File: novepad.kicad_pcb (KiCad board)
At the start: 2 copper layers, 99 x 59.5 mm, 16 parts, among them J101 NOVENA_LCD_CONN, J102 LP097QX1_CONN, J401 MOLEX_502250-8037, J402 MOLEX_502250-8037, U301 IT6251, U401 FT5816LPC

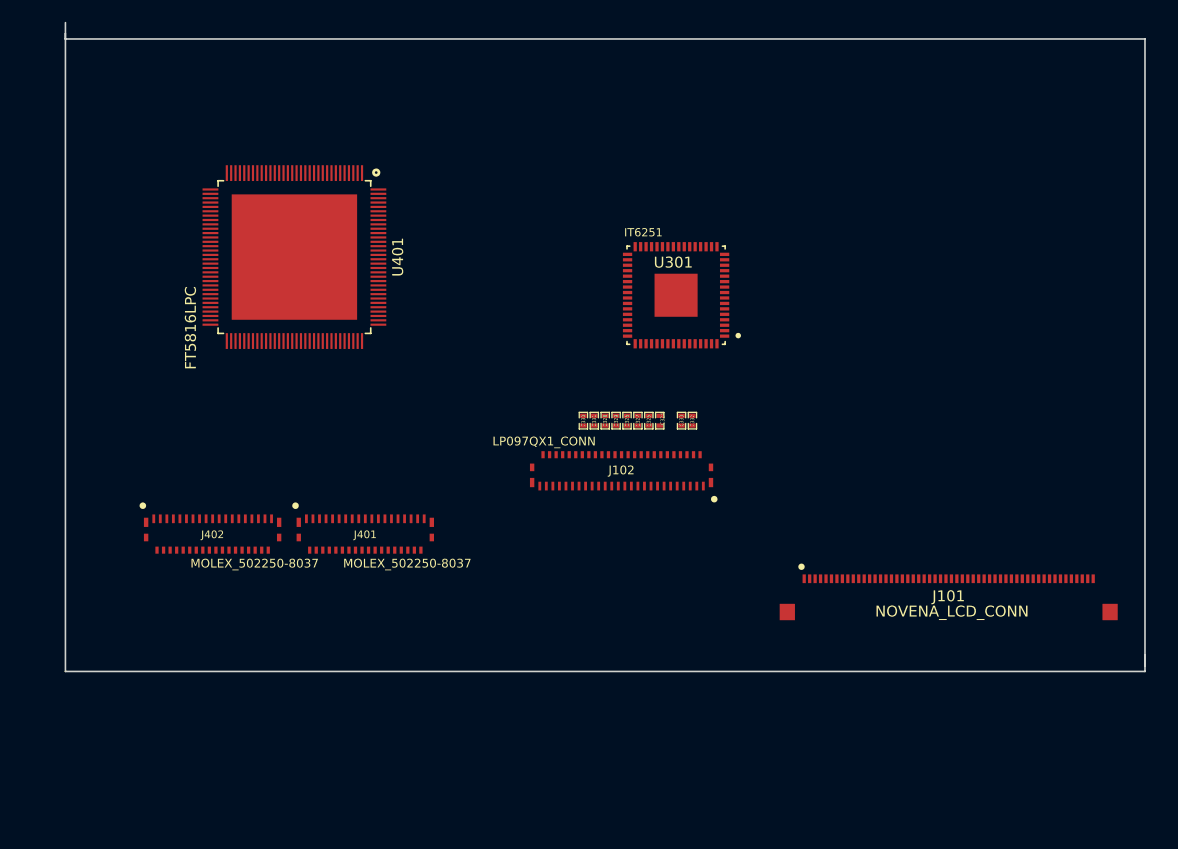
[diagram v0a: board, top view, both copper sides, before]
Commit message: First attempt at routing the high speed differential traces
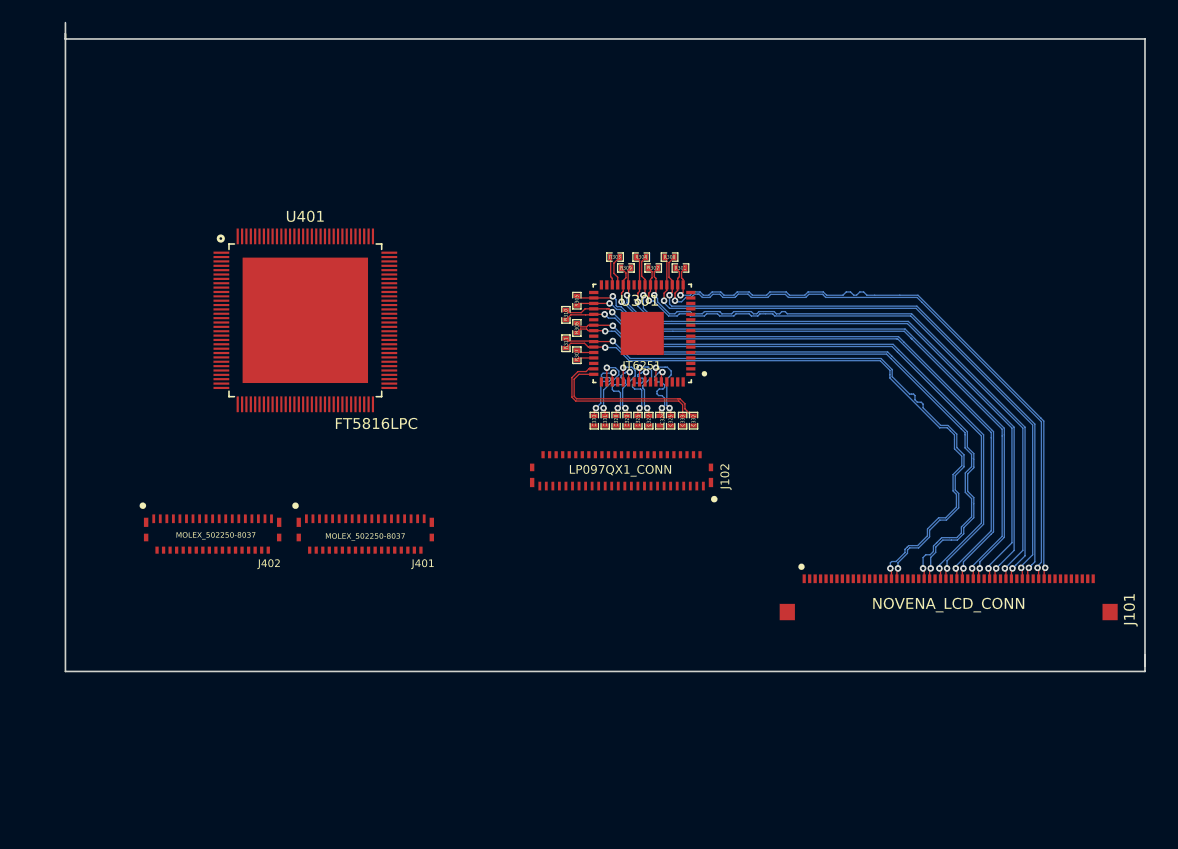
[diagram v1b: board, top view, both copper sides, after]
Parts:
- added R301: 100R 1%, SMD_Packages:SMD-0402_r, F.Cu at (144.4, 118.0)
- added R302: 100R 1%, SMD_Packages:SMD-0402_r, F.Cu at (141.9, 118.0)
- added R303: 100R 1%, SMD_Packages:SMD-0402_r, F.Cu at (138.4, 117.0)
- added R304: 100R 1%, SMD_Packages:SMD-0402_r, F.Cu at (140.8, 117.0)
- added R305: 100R 1%, SMD_Packages:SMD-0402_r, F.Cu at (134.9, 121.0)
- added R306: 100R 1%, SMD_Packages:SMD-0402_r, F.Cu at (134.9, 123.5)
- added R307: 100R 1%, SMD_Packages:SMD-0402_r, F.Cu at (134.9, 126.0)
- added R308: 100R 1%, SMD_Packages:SMD-0402_r, F.Cu at (143.4, 117.0)
- added R309: 100R 1%, SMD_Packages:SMD-0402_r, F.Cu at (139.4, 118.0)
- added R310: 100R 1%, SMD_Packages:SMD-0402_r, F.Cu at (133.9, 122.3)
- added R311: 100R 1%, SMD_Packages:SMD-0402_r, F.Cu at (133.9, 124.9)
- moved U401 5.89 mm to (110.0, 122.8), turned to 0 degrees
- moved U301 4.68 mm to (140.9, 124.0)
- moved C325 2.00 mm to (143.5, 132.0)
- moved C326 1.00 mm to (140.5, 132.0)
- moved C327 1.00 mm to (141.5, 132.0)
- moved C328 1.00 mm to (138.5, 132.0)
- moved C329 1.00 mm to (139.5, 132.0)
- moved C330 1.00 mm to (136.5, 132.0)
- moved C331 1.00 mm to (137.5, 132.0)
- moved C332 0.10 mm to (145.6, 132.0)
- moved C333 0.10 mm to (144.6, 132.0)
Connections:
- J101 pad 20: Net-(J101-Pad20) -> (no net)
- J101 pad 21: Net-(J101-Pad21) -> (no net)
- J101 pad 51: Net-(J101-Pad51) -> (no net)
- J101 pad 52: Net-(J101-Pad52) -> (no net)
- J101 pad 53: Net-(J101-Pad53) -> (no net)
- J101 pad 54: Net-(J101-Pad54) -> (no net)
- J102 pad 13: Net-(J102-Pad13) -> (no net)
- J102 pad 17: Net-(J102-Pad17) -> (no net)
- J102 pad 21: Net-(J102-Pad21) -> (no net)
- J102 pad 25: Net-(J102-Pad25) -> (no net)
- J102 pad 44: Net-(J102-Pad44) -> (no net)
- J102 pad 47: Net-(J102-Pad47) -> (no net)
- J102 pad 50: Net-(J102-Pad50) -> (no net)
- U301 pad 1: Net-(U301-Pad1) -> (no net)
- U301 pad 10: Net-(U301-Pad10) -> (no net)
- U301 pad 8: Net-(U301-Pad8) -> (no net)
- U301 pad 9: Net-(U301-Pad9) -> (no net)
- U401 pad 126: Net-(U401-Pad126) -> (no net)
- U401 pad 127: Net-(U401-Pad127) -> (no net)
- U401 pad 128: Net-(U401-Pad128) -> (no net)
- U401 pad 37: Net-(U401-Pad37) -> (no net)
- U401 pad 38: Net-(U401-Pad38) -> (no net)
- U401 pad 40: Net-(U401-Pad40) -> (no net)
- U401 pad 41: Net-(U401-Pad41) -> (no net)
- U401 pad 42: Net-(U401-Pad42) -> (no net)
- U401 pad 43: Net-(U401-Pad43) -> (no net)
- U401 pad 44: Net-(U401-Pad44) -> (no net)
- U401 pad 45: Net-(U401-Pad45) -> (no net)
- U401 pad 47: Net-(U401-Pad47) -> (no net)
- U401 pad 68: Net-(U401-Pad68) -> (no net)
- U401 pad 77: Net-(U401-Pad77) -> (no net)
- U401 pad 78: Net-(U401-Pad78) -> (no net)
- U401 pad 79: Net-(U401-Pad79) -> (no net)
- U401 pad 80: Net-(U401-Pad80) -> (no net)
- U401 pad 83: Net-(U401-Pad83) -> (no net)
- U401 pad 86: Net-(U401-Pad86) -> (no net)
- U401 pad 87: Net-(U401-Pad87) -> (no net)
- U401 pad 88: Net-(U401-Pad88) -> (no net)
- U401 pad 89: Net-(U401-Pad89) -> (no net)
- U401 pad 93: Net-(U401-Pad93) -> (no net)
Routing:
- net /LVDS to eDP Conversion/LVDS1_0_N: track 0.00 -> 58.5 mm, vias 0 -> 2
- net /LVDS to eDP Conversion/LVDS0_3_P: track 0.00 -> 58.4 mm, vias 0 -> 2
- net /LVDS to eDP Conversion/LVDS_CLK_P: track 0.00 -> 58.4 mm, vias 0 -> 2
- net /LVDS to eDP Conversion/LVDS_CLK_N: track 0.00 -> 58.2 mm, vias 0 -> 2
- net /LVDS to eDP Conversion/LVDS1_1_N: track 0.00 -> 58.0 mm, vias 0 -> 2
- net /LVDS to eDP Conversion/LVDS1_0_P: track 0.00 -> 57.8 mm, vias 0 -> 2
- net /LVDS to eDP Conversion/LVDS1_1_P: track 0.00 -> 57.7 mm, vias 0 -> 2
- net /LVDS to eDP Conversion/LVDS0_0_P: track 0.00 -> 57.6 mm, vias 0 -> 2
- net /LVDS to eDP Conversion/LVDS1_3_N: track 0.00 -> 57.6 mm, vias 0 -> 2
- net /LVDS to eDP Conversion/LVDS0_2_P: track 0.00 -> 57.5 mm, vias 0 -> 2
- net /LVDS to eDP Conversion/LVDS0_3_N: track 0.00 -> 57.5 mm, vias 0 -> 2
- net /LVDS to eDP Conversion/LVDS0_1_P: track 0.00 -> 57.5 mm, vias 0 -> 2
- net /LVDS to eDP Conversion/LVDS1_3_P: track 0.00 -> 57.3 mm, vias 0 -> 2
- net /LVDS to eDP Conversion/LVDS0_1_N: track 0.00 -> 57.3 mm, vias 0 -> 2
- net /LVDS to eDP Conversion/LVDS0_0_N: track 0.00 -> 57.2 mm, vias 0 -> 2
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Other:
- copper layers 2 -> 4
- net class Backlight added: clearance 0.2, trace_width 0.3, via_dia 0.7, via_drill 0.4
- net class Default: clearance 0.254 -> 0.2; trace_width 0.254 -> 0.2; via_dia 0.889 -> 0.7; via_drill 0.635 -> 0.4
- net class LVDS_LM3 added: clearance 0.1, trace_width 0.1, via_dia 0.6, via_drill 0.3
- net class LVDS_Unused added: clearance 0.1, trace_width 0.1, via_dia 0.7, via_drill 0.4
- net class Power added: clearance 0.3, trace_width 0.5, via_dia 1.2, via_drill 0.5
- net class eDP_ACC_LM0.2 added: clearance 0.1, trace_width 0.1, via_dia 0.6, via_drill 0.3
- net class eDP_AUX_LM0.5 added: clearance 0.1, trace_width 0.1, via_dia 0.6, via_drill 0.3
- net class eDP_LM0.5 added: clearance 0.1, trace_width 0.1, via_dia 0.6, via_drill 0.3
- rule trace_clearance: 0.254 -> 0.2
- rule trace_min: 0.254 -> 0.1
- rule via_min_drill: 0.508 -> 0.3
- rule via_min_size: 0.889 -> 0.6

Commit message: Super-zealous length matching version
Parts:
- added C201, C203, C207, C208: 4.7uF 25V, FT:1206, F.Cu at (137.5, 165.1)
- added C202, C204: 1uF 25V, FT:1206, F.Cu at (137.5, 165.1)
- added C205, C206: 100nF, FT:C0402, F.Cu at (137.5, 165.1)
- added C301: 100nF 25V X5R, SMD_Packages:SMD-0402_c, F.Cu at (147.8, 123.0)
- added C302: 100nF 25V X5R, SMD_Packages:SMD-0402_c, F.Cu at (135.7, 116.2)
- added C303: 100nF 25V X5R, SMD_Packages:SMD-0402_c, F.Cu at (147.8, 120.8)
- added C304: 1nF 25V X5R, SMD_Packages:SMD-0402_c, F.Cu at (135.7, 115.3)
- added C305: 100nF 25V X5R, SMD_Packages:SMD-0402_c, F.Cu at (134.5, 124.5)
- added C306: 100nF 25V X5R, SMD_Packages:SMD-0402_c, F.Cu at (147.8, 123.9)
- added C308: 1nF 25V X5R, SMD_Packages:SMD-0402_c, F.Cu at (147.8, 124.8)
- added C309: 100nF 25V X5R, SMD_Packages:SMD-0402_c, F.Cu at (140.1, 115.3)
- added C310: 100nF 25V X5R, SMD_Packages:SMD-0402_c, F.Cu at (144.3, 128.2)
- added C311: 100nF 25V X5R, SMD_Packages:SMD-0402_c, F.Cu at (134.5, 122.0)
- added C312: 1nF 25V X5R, SMD_Packages:SMD-0402_c, F.Cu at (145.3, 128.2)
- added C313: 100nF 25V X5R, SMD_Packages:SMD-0402_c, F.Cu at (135.7, 127.3)
- added C314: 100nF 25V X5R, SMD_Packages:SMD-0402_c, F.Cu at (138.7, 128.1)
- added C315: 1uF 25V X5R, SMD_Packages:SMD-0402_c, F.Cu at (147.8, 120.0)
- added C317: 100nF 25V X5R, SMD_Packages:SMD-0402_c, F.Cu at (142.7, 115.3)
- added C318: 100nF 25V X5R, SMD_Packages:SMD-0402_c, F.Cu at (134.5, 120.6)
- added C319, C323: 100nF 25V X5R, SMD_Packages:SMD-0402_c, F.Cu at (137.5, 165.1)
- added C321, C322, C405, C408: 27pF, FT:0603, F.Cu at (137.5, 165.1)
- added C401: 10uF 10V, FT:1206, F.Cu at (137.5, 165.1)
- added C402: 100nF 10V, SMD_Packages:SMD-0402_c, F.Cu at (137.5, 165.1)
- added C403, C404, C406, C407, C409: 1uF 10V, FT:1206, F.Cu at (137.5, 165.1)
- added C501, C502, C503, C504, C505, C506: 10uF 10V X5R, FT:1206, F.Cu at (137.5, 165.1)
- added D201, D202, D501: DFLS160-7, novepad:POWERDI123_DIODE, F.Cu at (137.5, 165.1)
- added L201, L202: 10uH NR4018T100M, novepad:NR4018_IND, F.Cu at (137.5, 165.1)
- added L401, L502, L503: BLM18KG121, FT:0603, F.Cu at (137.5, 165.1)
- added L501: 2.2uH CDRH3D23NP-2R2PC, novepad:CDRH3D23_IND, F.Cu at (137.5, 165.1)
- added R201, R402, R407: 0R DNP, FT:0603, F.Cu at (137.5, 165.1)
- added R202, R203: 51R, FT:0603, F.Cu at (137.5, 165.1)
- added R204, R205: 68K 1%, FT:0603, F.Cu at (137.5, 165.1)
- added R312, R314, R401, R406: 10K, FT:0603, F.Cu at (137.5, 165.1)
- added R313, R405: 10K DNP, FT:0603, F.Cu at (137.5, 165.1)
- added R315, R409: 1M, FT:0603, F.Cu at (137.5, 165.1)
- added R316: 820R 1%, FT:0603, F.Cu at (137.5, 165.1)
- added R317: 33R 1%, FT:0603, F.Cu at (137.5, 165.1)
- added R318: 100K DNP, FT:0603, F.Cu at (137.5, 165.1)
- added R319: 100K, FT:0603, F.Cu at (137.5, 165.1)
- added R403, R404: 22R, FT:0603, F.Cu at (137.5, 165.1)
- added R408: 10R, FT:0603, F.Cu at (137.5, 165.1)
- added R501: 10K 1%, FT:0603, F.Cu at (137.5, 165.1)
- added R502: 20K 1%, FT:0603, F.Cu at (137.5, 165.1)
- added REG501: NCP1117ST18T3G DNP, FT:SOT223, F.Cu at (137.5, 165.1)
- added REG502: LMR10510YSD, novepad:WSON6, F.Cu at (137.5, 165.1)
- added SJ101, SJ102, SJ501: SJ, FT:SJ_SHORTED, F.Cu at (137.5, 165.1)
- added TH201: NTPA7220LBMB0 1A 22R INRUSH LIMITER, novepad:PTH_2HOLE_5MM, F.Cu at (137.5, 165.1)
- added TP201, TP202, TP203, TP204, TP205, TP206, TP301, TP302, TP303, TP304, TP305, TP306, TP401, TP402, TP403, TP404, TP405, TP406, TP407, TP408, TP409, TP410, TP411, TP412, TP413, TP414, TP415, TP416, TP501, TP502: CONN_1, novepad:SMD_TEST_POINT, F.Cu at (137.5, 165.1)
- added U201, U202: TPS61181, novepad:QFN50P300X300X80-17N, F.Cu at (137.5, 165.1)
- added X301: 27MHz 50ppm, 8-18pF, ESR < 80ohm, FT:HC49UP, F.Cu at (137.5, 165.1)
- added X401: 12MHz 18pF, FT:HC49UP, F.Cu at (137.5, 165.1)
- moved R309 4.14 mm to (138.8, 113.9)
- moved R302 4.10 mm to (142.0, 113.9)
- moved R306 3.30 mm to (132.2, 121.6)
- moved R305 3.24 mm to (133.1, 118.3)
- moved R304 3.13 mm to (140.4, 113.9)
- moved R301 2.91 mm to (145.7, 115.4)
- moved R307 2.55 mm to (133.1, 124.2)
- moved R310 2.53 mm to (133.1, 119.9)
- moved R311 2.44 mm to (133.1, 122.6)
- moved U301 2.30 mm to (140.9, 121.7)
- moved R303 1.77 mm to (137.9, 115.3)
- moved R308 1.75 mm to (144.1, 115.4)
- moved C324 0.40 mm to (142.5, 132.4)
- moved C325 0.40 mm to (143.5, 132.4)
- moved C326 0.40 mm to (140.5, 132.4)
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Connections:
- U401 pad 1: /Capacitive Touch (Optional)/TX8 -> /Capacitive Touch (Optional)/TX33
- U401 pad 10: /Capacitive Touch (Optional)/TX17 -> /Capacitive Touch (Optional)/TX24
- U401 pad 100: /Capacitive Touch (Optional)/RX5 -> /Capacitive Touch (Optional)/RX26
- U401 pad 101: /Capacitive Touch (Optional)/RX6 -> /Capacitive Touch (Optional)/RX25
- U401 pad 102: /Capacitive Touch (Optional)/RX7 -> /Capacitive Touch (Optional)/RX24
- U401 pad 103: /Capacitive Touch (Optional)/RX8 -> /Capacitive Touch (Optional)/RX23
- U401 pad 104: /Capacitive Touch (Optional)/RX9 -> /Capacitive Touch (Optional)/RX22
- U401 pad 105: /Capacitive Touch (Optional)/RX10 -> /Capacitive Touch (Optional)/RX21
- U401 pad 106: /Capacitive Touch (Optional)/RX11 -> /Capacitive Touch (Optional)/RX20
- U401 pad 107: /Capacitive Touch (Optional)/RX12 -> /Capacitive Touch (Optional)/RX19
- U401 pad 108: /Capacitive Touch (Optional)/RX13 -> /Capacitive Touch (Optional)/RX18
- U401 pad 109: /Capacitive Touch (Optional)/RX14 -> /Capacitive Touch (Optional)/RX17
- U401 pad 11: /Capacitive Touch (Optional)/TX18 -> /Capacitive Touch (Optional)/TX23
- U401 pad 110: /Capacitive Touch (Optional)/RX15 -> /Capacitive Touch (Optional)/RX16
- U401 pad 111: /Capacitive Touch (Optional)/RX16 -> /Capacitive Touch (Optional)/RX15
- U401 pad 112: /Capacitive Touch (Optional)/RX17 -> /Capacitive Touch (Optional)/RX14
- U401 pad 113: /Capacitive Touch (Optional)/RX18 -> /Capacitive Touch (Optional)/RX13
- U401 pad 119: /Capacitive Touch (Optional)/TX1 -> /Capacitive Touch (Optional)/TX40
- U401 pad 12: /Capacitive Touch (Optional)/TX19 -> /Capacitive Touch (Optional)/TX22
- U401 pad 120: /Capacitive Touch (Optional)/TX2 -> /Capacitive Touch (Optional)/TX39
- U401 pad 121: /Capacitive Touch (Optional)/TX3 -> /Capacitive Touch (Optional)/TX38
- U401 pad 122: /Capacitive Touch (Optional)/TX4 -> /Capacitive Touch (Optional)/TX37
- U401 pad 123: /Capacitive Touch (Optional)/TX5 -> /Capacitive Touch (Optional)/TX36
- U401 pad 124: /Capacitive Touch (Optional)/TX6 -> /Capacitive Touch (Optional)/TX35
- U401 pad 125: /Capacitive Touch (Optional)/TX7 -> /Capacitive Touch (Optional)/TX34
- U401 pad 13: /Capacitive Touch (Optional)/TX20 -> /Capacitive Touch (Optional)/TX21
- U401 pad 14: /Capacitive Touch (Optional)/TX21 -> /Capacitive Touch (Optional)/TX20
- U401 pad 15: /Capacitive Touch (Optional)/TX22 -> /Capacitive Touch (Optional)/TX19
- U401 pad 16: /Capacitive Touch (Optional)/TX23 -> /Capacitive Touch (Optional)/TX18
- U401 pad 2: /Capacitive Touch (Optional)/TX9 -> /Capacitive Touch (Optional)/TX32
- U401 pad 20: /Capacitive Touch (Optional)/TX24 -> /Capacitive Touch (Optional)/TX17
- U401 pad 21: /Capacitive Touch (Optional)/TX25 -> /Capacitive Touch (Optional)/TX16
- U401 pad 22: /Capacitive Touch (Optional)/TX26 -> /Capacitive Touch (Optional)/TX15
- U401 pad 23: /Capacitive Touch (Optional)/TX27 -> /Capacitive Touch (Optional)/TX14
- U401 pad 24: /Capacitive Touch (Optional)/TX28 -> /Capacitive Touch (Optional)/TX13
- U401 pad 25: /Capacitive Touch (Optional)/TX29 -> /Capacitive Touch (Optional)/TX12
- U401 pad 26: /Capacitive Touch (Optional)/TX30 -> /Capacitive Touch (Optional)/TX11
- U401 pad 27: /Capacitive Touch (Optional)/TX31 -> /Capacitive Touch (Optional)/TX10
- U401 pad 28: /Capacitive Touch (Optional)/TX32 -> /Capacitive Touch (Optional)/TX9
- U401 pad 29: /Capacitive Touch (Optional)/TX33 -> /Capacitive Touch (Optional)/TX8
- U401 pad 3: /Capacitive Touch (Optional)/TX10 -> /Capacitive Touch (Optional)/TX31
- U401 pad 30: /Capacitive Touch (Optional)/TX34 -> /Capacitive Touch (Optional)/TX7
- U401 pad 31: /Capacitive Touch (Optional)/TX35 -> /Capacitive Touch (Optional)/TX6
- U401 pad 32: /Capacitive Touch (Optional)/TX36 -> /Capacitive Touch (Optional)/TX5
- U401 pad 33: /Capacitive Touch (Optional)/TX37 -> /Capacitive Touch (Optional)/TX4
- U401 pad 34: /Capacitive Touch (Optional)/TX38 -> /Capacitive Touch (Optional)/TX3
- U401 pad 35: /Capacitive Touch (Optional)/TX39 -> /Capacitive Touch (Optional)/TX2
- U401 pad 36: /Capacitive Touch (Optional)/TX40 -> /Capacitive Touch (Optional)/TX1
- U401 pad 4: /Capacitive Touch (Optional)/TX11 -> /Capacitive Touch (Optional)/TX30
- U401 pad 5: /Capacitive Touch (Optional)/TX12 -> /Capacitive Touch (Optional)/TX29
- U401 pad 54: /Capacitive Touch (Optional)/RX30 -> /Capacitive Touch (Optional)/RX1
- U401 pad 55: /Capacitive Touch (Optional)/RX29 -> /Capacitive Touch (Optional)/RX2
- U401 pad 56: /Capacitive Touch (Optional)/RX28 -> /Capacitive Touch (Optional)/RX3
- U401 pad 57: /Capacitive Touch (Optional)/RX27 -> /Capacitive Touch (Optional)/RX4
- U401 pad 58: /Capacitive Touch (Optional)/RX26 -> /Capacitive Touch (Optional)/RX5
- U401 pad 59: /Capacitive Touch (Optional)/RX25 -> /Capacitive Touch (Optional)/RX6
- U401 pad 6: /Capacitive Touch (Optional)/TX13 -> /Capacitive Touch (Optional)/TX28
- U401 pad 60: /Capacitive Touch (Optional)/RX24 -> /Capacitive Touch (Optional)/RX7
- U401 pad 61: /Capacitive Touch (Optional)/RX23 -> /Capacitive Touch (Optional)/RX8
- U401 pad 62: /Capacitive Touch (Optional)/RX22 -> /Capacitive Touch (Optional)/RX9
- U401 pad 63: /Capacitive Touch (Optional)/RX21 -> /Capacitive Touch (Optional)/RX10
- U401 pad 64: /Capacitive Touch (Optional)/RX20 -> /Capacitive Touch (Optional)/RX11
- U401 pad 65: /Capacitive Touch (Optional)/RX19 -> /Capacitive Touch (Optional)/RX12
- U401 pad 7: /Capacitive Touch (Optional)/TX14 -> /Capacitive Touch (Optional)/TX27
- U401 pad 8: /Capacitive Touch (Optional)/TX15 -> /Capacitive Touch (Optional)/TX26
- U401 pad 9: /Capacitive Touch (Optional)/TX16 -> /Capacitive Touch (Optional)/TX25
- U401 pad 96: /Capacitive Touch (Optional)/RX1 -> /Capacitive Touch (Optional)/RX30
- U401 pad 97: /Capacitive Touch (Optional)/RX2 -> /Capacitive Touch (Optional)/RX29
- U401 pad 98: /Capacitive Touch (Optional)/RX3 -> /Capacitive Touch (Optional)/RX28
- U401 pad 99: /Capacitive Touch (Optional)/RX4 -> /Capacitive Touch (Optional)/RX27
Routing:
- net +1.8VA: track 0.00 -> 32.3 mm, vias 0 -> 2
- net /LVDS to eDP Conversion/eDP_AUX_P: track 0.00 -> 5.85 mm, vias 0 -> 2
- net /LVDS to eDP Conversion/eDP_AUX_N: track 0.00 -> 5.70 mm, vias 0 -> 2
- net +3.3V: track 0.00 -> 5.13 mm, vias 0 -> 2
- net +1.8V: track 0.00 -> 4.87 mm, vias 0 -> 1
- net /LVDS to eDP Conversion/eDP_LANE1_N: track 0.00 -> 3.62 mm
- net /LVDS to eDP Conversion/eDP_LANE3_N: track 0.00 -> 3.61 mm
- net /LVDS to eDP Conversion/eDP_LANE2_N: track 0.00 -> 3.59 mm
- net /LVDS to eDP Conversion/eDP_LANE0_N: track 0.00 -> 3.58 mm
- net /LVDS to eDP Conversion/eDP_LANE1_P: track 0.00 -> 3.57 mm
- net /LVDS to eDP Conversion/eDP_LANE0_P: track 0.00 -> 3.56 mm
- net /LVDS to eDP Conversion/eDP_LANE3_P: track 0.00 -> 3.55 mm
- net /LVDS to eDP Conversion/eDP_LANE2_P: track 0.00 -> 3.55 mm
- net /LVDS to eDP Conversion/RXNE1: track 2.92 -> 0.00 mm
- net /LVDS to eDP Conversion/AUX_P: track 15.5 -> 18.4 mm
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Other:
- net class Power: clearance 0.3 -> 0.2
- net class eDP_AUX_OUT_LM0.5 added: clearance 0.2, trace_width 0.2, via_dia 0.7, via_drill 0.4
